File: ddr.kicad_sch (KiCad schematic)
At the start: 53 parts, among them U801 MT41K256M16TW

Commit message: DDR: Replace series termination with parallel
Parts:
- removed R802: 0 Ω, perfect_footprints:R_0201_0603Metric, symbol Device:R
- removed unit 3 of U801
- added C801, C802, C803: 10 µF, Capacitor_SMD:C_0603_1608Metric, symbol Device:C
- added C812, C813, C814, C817, C818, C819, C822, C823, C824, C827, C828, C829, C833, C834, C835: 1 µF, perfect_footprints:C_0201_0603Metric, symbol Device:C
- added R821: 49.9 Ω, perfect_footprints:R_0201_0603Metric, symbol Device:R
- R803, R804, R805, R806, R807, R808, R809, R810, R811, R812, R813, R814, R815, R816, R817, R818, R819, R820, R822, R823, R824, R825, R826, R827, R828: value 0 Ω -> 49.9 Ω; Digi-Key Part Number P15979CT-ND -> P123049CT-ND; MPN ERJ-1GN0R00C -> ERJ-1GNF49R9C; Power rating (none) -> 0.05 W; Tolerance (none) -> 1 %
- U801: Digi-Key Part Number_1 (none) -> 557-1792-ND; MPN_1 (none) -> MT41K256M16TW-107:P; Manufacturer_1 (none) -> Micron Technology Inc.
- renumbered C801 to C804, C802 to C805, C803 to C806, C804 to C807, C805 to C808, C806 to C809, C807 to C810, C808 to C811, C809 to C815, C810 to C816, C811 to C820, C812 to C821, C813 to C825, C814 to C826, C815 to C830, C816 to C831, C817 to C832, C818 to C836, C819 to C837, C820 to C838, C821 to C839, C822 to C840, R821 to R801, R801 to R802
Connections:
- net A0 is gone; now on net DDR.A0: U801.N3 (A0)
- net CAS_N is gone; now on net DDR.CAS_N: R823.2
- net CKE is gone; now on net DDR.CKE: R825.2, R830.1
- net CS_N is gone; now on net DDR.CS_N: R824.2
- net ODT is gone; now on net DDR.ODT: R827.2
- net RAS_N is gone; now on net DDR.RAS_N: R822.2
- net RST_N is gone; now on net DDR.RST_N: R828.2, R829.1
- net WE_N is gone; now on net DDR.WE_N: R826.2
- net DDR.A0: now also R803.2
- net DDR.A1: now also R804.2, U801.P7 (A1); no longer R803.1
- net DDR.A10: now also R813.2, U801.L7 (A10/AP); no longer R812.1
- net DDR.A11: now also R814.2, U801.R7 (A11); no longer R813.1
- net DDR.A12: now also R815.2, U801.N7 (A12/BC_N); no longer R814.1
- net DDR.A13: now also R816.2, U801.T3 (A13); no longer R815.1
- net DDR.A14: now also R817.2, U801.T7 (A14); no longer R816.1
- net DDR.A15: now also R818.2, U801.M7 (NC); no longer R817.1
- net DDR.A2: now also R805.2, U801.P3 (A2); no longer R804.1
- net DDR.A3: now also R806.2, U801.N2 (A3); no longer R805.1
- net DDR.A4: now also R807.2, U801.P8 (A4); no longer R806.1
- net DDR.A5: now also R808.2, U801.P2 (A5); no longer R807.1
- net DDR.A6: now also R809.2, U801.R8 (A6); no longer R808.1
- net DDR.A7: now also R810.2, U801.R2 (A7); no longer R809.1
- net DDR.A8: now also R811.2, U801.T8 (A8); no longer R810.1
- net DDR.A9: now also R812.2, U801.R3 (A9); no longer R811.1
- net DDR.BA0: now also R819.2, U801.M2 (BA0); no longer R818.1
- net DDR.BA1: now also R820.2, U801.N8 (BA1); no longer R819.1
- net DDR.BA2: now also U801.M3 (BA2), R821.2; no longer R820.1
- net DDR.CAS_N: now also U801.K3 (CAS_N); no longer R823.1
- net DDR.CKE: now also U801.K9 (CKE); no longer R825.1
- net DDR.CS_N: now also U801.L2 (CS_N); no longer R824.1
- net DDR.ODT: now also U801.K1 (ODT); no longer R827.1
- net DDR.RAS_N: now also U801.J3 (RAS_N); no longer R822.1
- net DDR.RST_N: now also U801.T2 (RESET_N); no longer R828.1
- net DDR.WE_N: now also U801.L3 (WE_N); no longer R826.1
- net GND: now also C801.2, C802.2, C803.2, C812.2, C813.2, C814.2, C817.2, C818.2, C819.2, C822.2, C823.2, C824.2, C827.2, C828.2, C829.2, C833.2, C834.2, C835.2
- removed net A1: R803.2, U801.P7 (A1)
- removed net A10: R812.2, U801.L7 (A10/AP)
- removed net A11: R813.2, U801.R7 (A11)
- removed net A12: R814.2, U801.N7 (A12/BC_N)
- removed net A13: R815.2, U801.T3 (A13)
- removed net A14: R816.2, U801.T7 (A14)
- removed net A15: R817.2, U801.M7 (NC)
- removed net A2: R804.2, U801.P3 (A2)
- removed net A3: R805.2, U801.N2 (A3)
- removed net A4: R806.2, U801.P8 (A4)
- removed net A5: R807.2, U801.P2 (A5)
- removed net A6: R808.2, U801.R8 (A6)
- removed net A7: R809.2, U801.R2 (A7)
- removed net A8: R810.2, U801.T8 (A8)
- removed net A9: R811.2, U801.R3 (A9)
- removed net BA0: R818.2, U801.M2 (BA0)
- removed net BA1: R819.2, U801.N8 (BA1)
- removed net BA2: R820.2, U801.M3 (BA2)
- new net VTT_DDR: C801.1, C802.1, C803.1, C812.1, C813.1, C814.1, C817.1, C818.1, C819.1, C822.1, C823.1, C824.1, C827.1, C828.1, C829.1, C833.1, C834.1, C835.1, R803.1, R804.1, R805.1, R806.1, R807.1, R808.1, R809.1, R810.1, R811.1, R812.1, R813.1, R814.1, R815.1, R816.1, R817.1, R818.1, R819.1, R820.1, R821.1, R822.1, R823.1, R824.1, R825.1, R826.1, R827.1, R828.1
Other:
- note added: "1 µF x termination resistor / 2"
- note added: "Bulk decoupling"
- note added: "Control/address and data"
- note added: "Place near MPU."
- note added: "Place near termination resistors."
- note added: "Place near the DDR."
- note added: "Route DDR_CA as 50 Ω single-ended."
- note added: "Route DDR_CLK as 100 Ω differential."
- note added: "Route DDR_U as 50 Ω single-ended."
- note added: "Termination"
- note removed: "Addressing and data"
- note removed: "Control"
- note removed: "Route DDR as 50 Ω for single-ended, 100 Ω for differential."
- moved on the sheet: C804, C805, C806, C807, C808, C809, C810, C811, C815, C816, C820, C821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

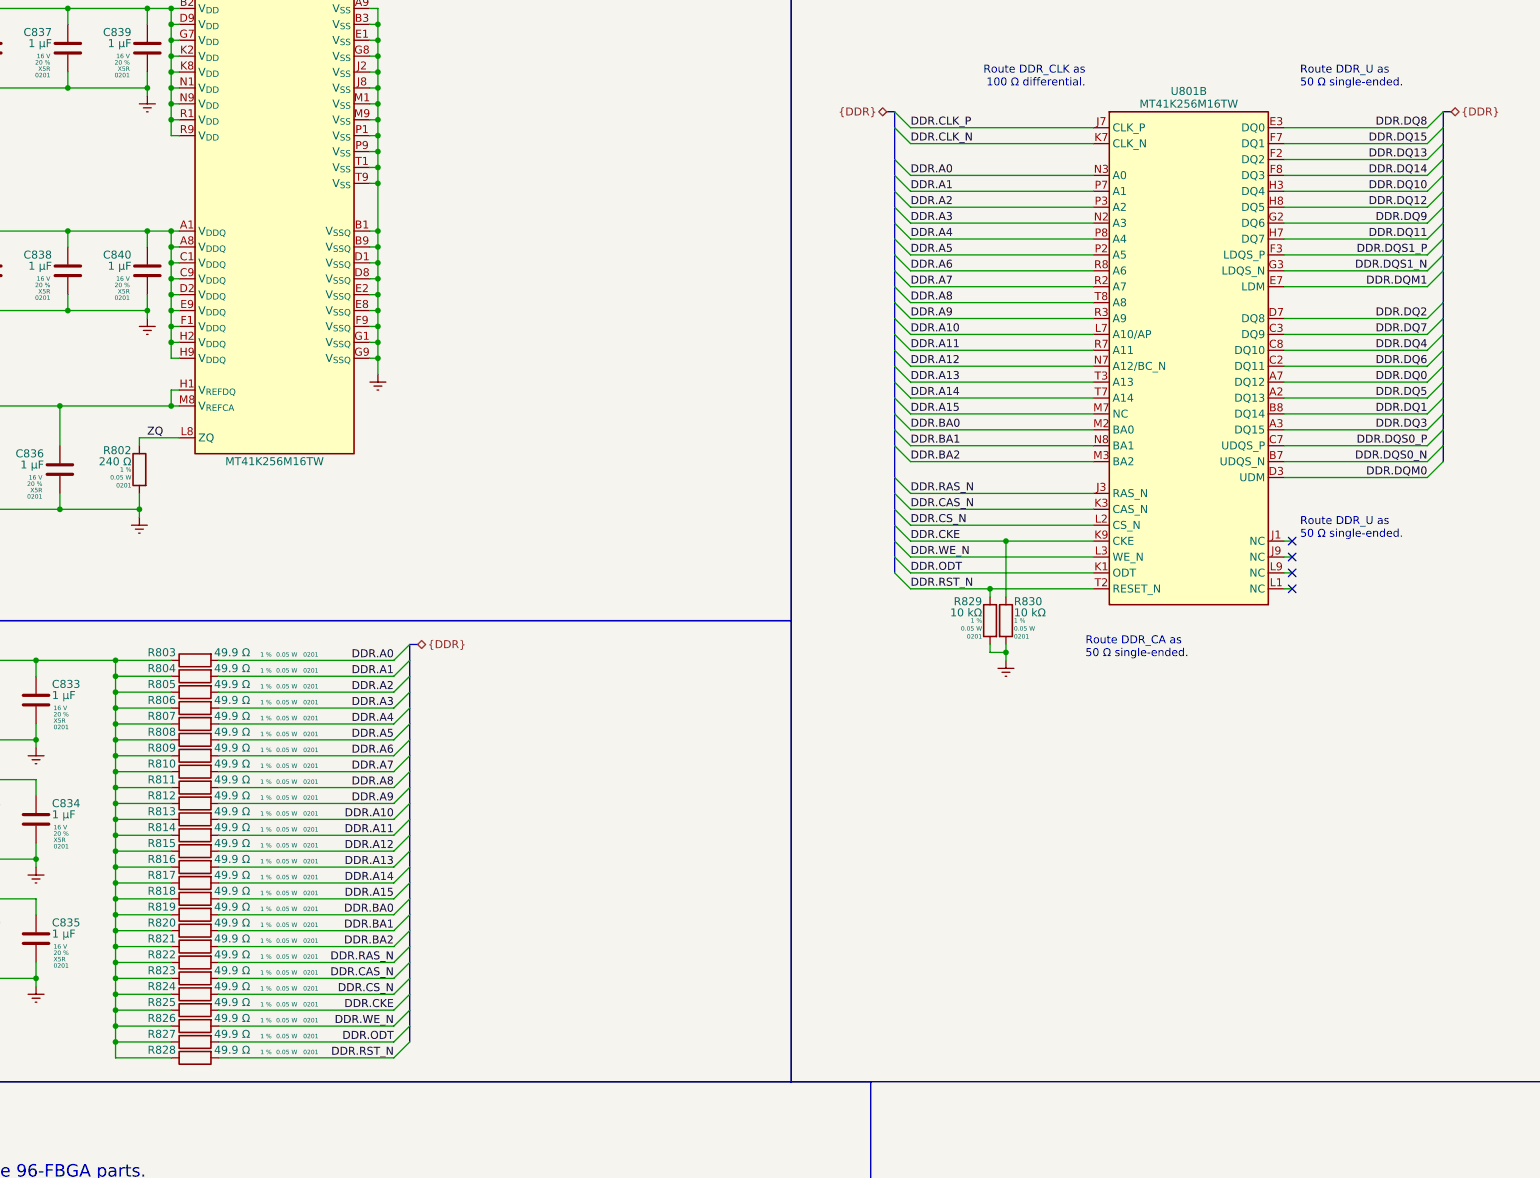
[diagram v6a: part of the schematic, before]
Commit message: Start laying out ddr vtt termination
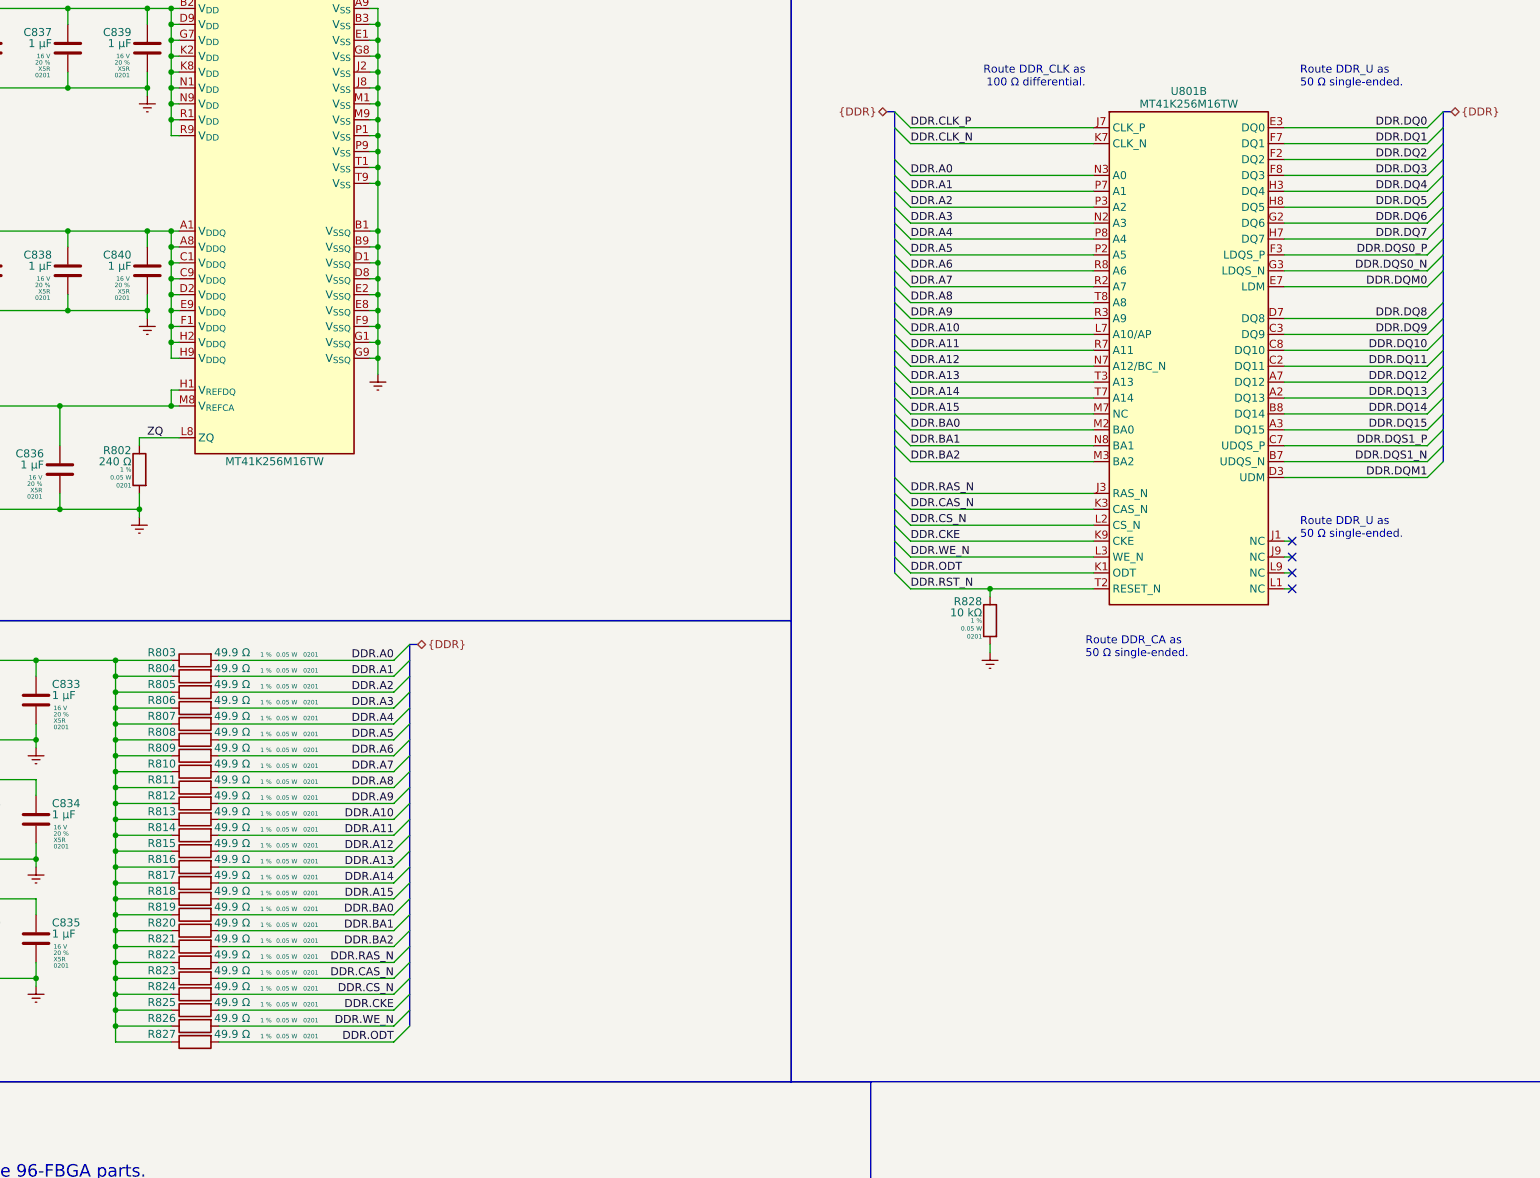
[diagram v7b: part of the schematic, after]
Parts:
- removed R828: 49.9 Ω, perfect_footprints:R_0201_0603Metric, symbol Device:R
- removed R830: 10 kΩ, perfect_footprints:R_0201_0603Metric, symbol Device:R
- renumbered R829 to R828
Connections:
- net DDR.DQ0: now also U801.E3 (DQ0); no longer U801.A7 (DQ12)
- net DDR.DQ1: now also U801.F7 (DQ1); no longer U801.B8 (DQ14)
- net DDR.DQ10: now also U801.C8 (DQ10); no longer U801.H3 (DQ4)
- net DDR.DQ11: now also U801.C2 (DQ11); no longer U801.H7 (DQ7)
- net DDR.DQ12: now also U801.A7 (DQ12); no longer U801.H8 (DQ5)
- net DDR.DQ13: now also U801.A2 (DQ13); no longer U801.F2 (DQ2)
- net DDR.DQ14: now also U801.B8 (DQ14); no longer U801.F8 (DQ3)
- net DDR.DQ15: now also U801.A3 (DQ15); no longer U801.F7 (DQ1)
- net DDR.DQ2: now also U801.F2 (DQ2); no longer U801.D7 (DQ8)
- net DDR.DQ3: now also U801.F8 (DQ3); no longer U801.A3 (DQ15)
- net DDR.DQ4: now also U801.H3 (DQ4); no longer U801.C8 (DQ10)
- net DDR.DQ5: now also U801.H8 (DQ5); no longer U801.A2 (DQ13)
- net DDR.DQ6: now also U801.G2 (DQ6); no longer U801.C2 (DQ11)
- net DDR.DQ7: now also U801.H7 (DQ7); no longer U801.C3 (DQ9)
- net DDR.DQ8: now also U801.D7 (DQ8); no longer U801.E3 (DQ0)
- net DDR.DQ9: now also U801.C3 (DQ9); no longer U801.G2 (DQ6)
- net DDR.DQM0: now also U801.E7 (LDM); no longer U801.D3 (UDM)
- net DDR.DQM1: now also U801.D3 (UDM); no longer U801.E7 (LDM)
- net DDR.DQS0_N: now also U801.G3 (LDQS_N); no longer U801.B7 (UDQS_N)
- net DDR.DQS0_P: now also U801.F3 (LDQS_P); no longer U801.C7 (UDQS_P)
- net DDR.DQS1_N: now also U801.B7 (UDQS_N); no longer U801.G3 (LDQS_N)
- net DDR.DQS1_P: now also U801.C7 (UDQS_P); no longer U801.F3 (LDQS_P)
